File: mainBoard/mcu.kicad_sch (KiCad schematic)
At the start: 36 parts, among them J2 USB_A, SW2 SW_SPDT, SW3 SW_Push, SW4 SW_Push, U19 23LC1024-I/ST, U5 USBLC6-2SC6, U6 STM32F413RHT6, Y1 RH100-48.000-10-F-1015-X-TR-N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

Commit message: add NOR flash for UI
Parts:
- added C55: 100nF, Capacitor_SMD:C_0603_1608Metric_Pad1.08x0.95mm_HandSolder, symbol Device:C
- added U22: W25Q64JVSSIM TR, Package_SO:SOIC-8_5.3x5.3mm_P1.27mm, symbol Memory_Flash:W25Q16JVSS
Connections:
- net +3.3V: now also C55.1, U22.8 (VCC)
- net GND: now also C55.2, U22.4 (GND)
- net QSPI_SCK: now also U22.6 (CLK)
- net QSPI_SIO0: now also U22.5 (DI/IO_{0})
- net QSPI_SIO1: now also U22.2 (DO/IO_{1})
- net QSPI_SIO2: now also U22.3 (~{WP}/IO_{2})
- net QSPI_SIO3: now also U22.7 (~{HOLD}/~{RESET}/IO_{3})
- new net QSPI_ROM_CS: U22.1 (~{CS})
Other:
- note added: "8MB NOR Flash"
- moved on the sheet: C21, C22, C23, C24, C25, C26, C27, C28, C29, C30, C31, R18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

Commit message: change to 16MB ROM
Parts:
- U22: value W25Q64JVSSIM TR -> W25Q128JVSIQ TR
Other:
- note added: "16MB NOR Flash"
- note removed: "8MB NOR Flash"
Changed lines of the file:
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@@
 		)
 	)
-	(text "8MB NOR Flash"
+	(text "16MB NOR Flash"
 		(exclude_from_sim no)
 		(at 85.852 146.812 0)
@@
 			)
 		)
-		(property "Value" "W25Q64JVSSIM TR"
+		(property "Value" "W25Q128JVSIQ TR"
 			(at 71.12 123.1899 0)
 			(show_name no)

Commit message: working on pcb layout, change to soic sram
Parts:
- U19: value 23LC1024-I/ST -> 23LC1024-E/SN; footprint Package_SO:TSSOP-8_4.4x3mm_P0.65mm -> Package_SO:SOIC-8_5.3x5.3mm_P1.27mm
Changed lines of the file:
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@@
 			)
 		)
-		(property "Value" "23LC1024-I/ST"
+		(property "Value" "23LC1024-E/SN"
 			(at 64.135 180.975 0)
 			(show_name no)
@@
 			)
 		)
-		(property "Footprint" "Package_SO:TSSOP-8_4.4x3mm_P0.65mm"
+		(property "Footprint" "Package_SO:SOIC-8_5.3x5.3mm_P1.27mm"
 			(at 55.88 195.58 0)
 			(hide yes)

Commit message: work on layout
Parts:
- removed NT2: NetTie_2, NetTie:NetTie-2_SMD_Pad0.5mm, symbol Device:NetTie_2
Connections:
- net HSE_GND is gone; now on net GND: C22.2, C23.2
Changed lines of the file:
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@@
 	(wire
 		(pts
+			(xy 196.85 179.07) (xy 196.85 185.42)
+		)
+		(stroke
+			(width 0)
+			(type default)
+		)
+	)
+	(wire
+		(pts
 			(xy 157.48 111.76) (xy 153.67 111.76)
 		)
@@
 	(wire
 		(pts
-			(xy 196.85 179.07) (xy 196.85 180.34)
-		)
-		(stroke
-			(width 0)
-			(type default)
-		)
-	)
-	(wire
-		(pts
 			(xy 45.72 237.49) (xy 57.15 237.49)
 		)
@@
 					(unit 1)
 				)
-			)
-		)
-	)
-	(symbol
-		(lib_id "Device:NetTie_2")
-		(at 196.85 182.88 90)
-		(unit 1)
-		(body_style 1)
-		(exclude_from_sim no)
-		(in_bom no)
-		(on_board yes)
-		(in_pos_files yes)
-		(dnp no)
-		(fields_autoplaced yes)
-		(property "Reference" "NT2"
-			(at 191.77 182.88 0)
-			(hide yes)
-			(show_name no)
-			(do_not_autoplace no)
-			(effects
-				(font
-					(size 1.27 1.27)
-				)
-			)
-		)
-		(property "Value" "NetTie_2"
-			(at 194.31 182.88 0)
-			(hide yes)
-			(show_name no)
-			(do_not_autoplace no)
-			(effects
-				(font
-					(size 1.27 1.27)
-				)
-			)
-		)
-		(property "Footprint" "NetTie:NetTie-2_SMD_Pad0.5mm"
-			(at 196.85 182.88 0)
-			(hide yes)
-			(show_name no)
-			(do_not_autoplace no)
-			(effects
-				(font
-					(size 1.27 1.27)
-				)
-			)
-		)
-		(property "Datasheet" ""
-			(at 196.85 182.88 0)
-			(hide yes)
-			(show_name no)
-			(do_not_autoplace no)
-			(effects
-				(font
-					(size 1.27 1.27)
-				)
-			)
-		)
-		(property "Description" "Net tie, 2 pins"
-			(at 196.85 182.88 0)
-			(hide yes)
-			(show_name no)
-			(do_not_autoplace no)
-			(effects
-				(font
-					(size 1.27 1.27)
-				)
-			)
-		)
-		(pin "1"
-		)
-		(pin "2"
-		)
-		(instances
-			(project "mainBoard"
-				(path "/0650c7a8-acba-429c-9f8e-eec0baf0bc1c/fede4c36-00cc-4d3d-b71c-5243ba232202/7d5a1283-086b-46b0-8df7-a9850521fb5e"
-					(reference "NT2")
-					(unit 1)
-				)

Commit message: work on layout
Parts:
- removed NT1: NetTie_2, NetTie:NetTie-2_SMD_Pad0.5mm, symbol Device:NetTie_2
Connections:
- net STM_VREF is gone; now on net +3.3VA: U6.13 (VREF+)
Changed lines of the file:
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@@
 	(wire
 		(pts
-			(xy 140.97 129.54) (xy 142.24 129.54)
+			(xy 140.97 129.54) (xy 266.7 129.54)
 		)
 		(stroke
@@
 	(wire
 		(pts
-			(xy 147.32 129.54) (xy 266.7 129.54)
-		)
-		(stroke
-			(width 0)
-			(type default)
-		)
-	)
-	(wire
-		(pts
 			(xy 250.19 66.04) (xy 250.19 67.31)
 		)
@@
 					(unit 1)
 				)
-			)
-		)
-	)
-	(symbol
-		(lib_id "Device:NetTie_2")
-		(at 144.78 129.54 180)
-		(unit 1)
-		(body_style 1)
-		(exclude_from_sim no)
-		(in_bom no)
-		(on_board yes)
-		(in_pos_files yes)
-		(dnp no)
-		(fields_autoplaced yes)
-		(property "Reference" "NT1"
-			(at 144.78 134.62 0)
-			(hide yes)
-			(show_name no)
-			(do_not_autoplace no)
-			(effects
-				(font
-					(size 1.27 1.27)
-				)
-			)
-		)
-		(property "Value" "NetTie_2"
-			(at 144.78 132.08 0)
-			(hide yes)
-			(show_name no)
-			(do_not_autoplace no)
-			(effects
-				(font
-					(size 1.27 1.27)
-				)
-			)
-		)
-		(property "Footprint" "NetTie:NetTie-2_SMD_Pad0.5mm"
-			(at 144.78 129.54 0)
-			(hide yes)
-			(show_name no)
-			(do_not_autoplace no)
-			(effects
-				(font
-					(size 1.27 1.27)
-				)
-			)
-		)
-		(property "Datasheet" ""
-			(at 144.78 129.54 0)
-			(hide yes)
-			(show_name no)
-			(do_not_autoplace no)
-			(effects
-				(font
-					(size 1.27 1.27)
-				)
-			)
-		)
-		(property "Description" "Net tie, 2 pins"
-			(at 144.78 129.54 0)
-			(hide yes)
-			(show_name no)
-			(do_not_autoplace no)
-			(effects
-				(font
-					(size 1.27 1.27)
-				)
-			)
-		)
-		(pin "1"
-		)
-		(pin "2"
-		)
-		(instances
-			(project "mainBoard"
-				(path "/0650c7a8-acba-429c-9f8e-eec0baf0bc1c/fede4c36-00cc-4d3d-b71c-5243ba232202/7d5a1283-086b-46b0-8df7-a9850521fb5e"
-					(reference "NT1")
-					(unit 1)
-				)

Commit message: work on board layout
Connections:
- net TC3_ADC: now also U6.24 (PC4); no longer U6.26 (PB0)
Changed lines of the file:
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@@
 	(global_label "TC3_ADC"
 		(shape input)
-		(at 302.26 162.56 0)
+		(at 266.7 157.48 180)
 		(fields_autoplaced yes)
 		(effects
@@
 				(size 1.27 1.27)
 			)
-			(justify left)
+			(justify right)
 		)
 		(property "Intersheetrefs" "${INTERSHEET_REFS}"
-			(at 311.8581 162.56 0)
+			(at 255.6715 157.48 0)
 			(hide yes)
 			(show_name no)
@@
 					(size 1.27 1.27)
 				)
-				(justify left)
+				(justify right)
 			)
 		)

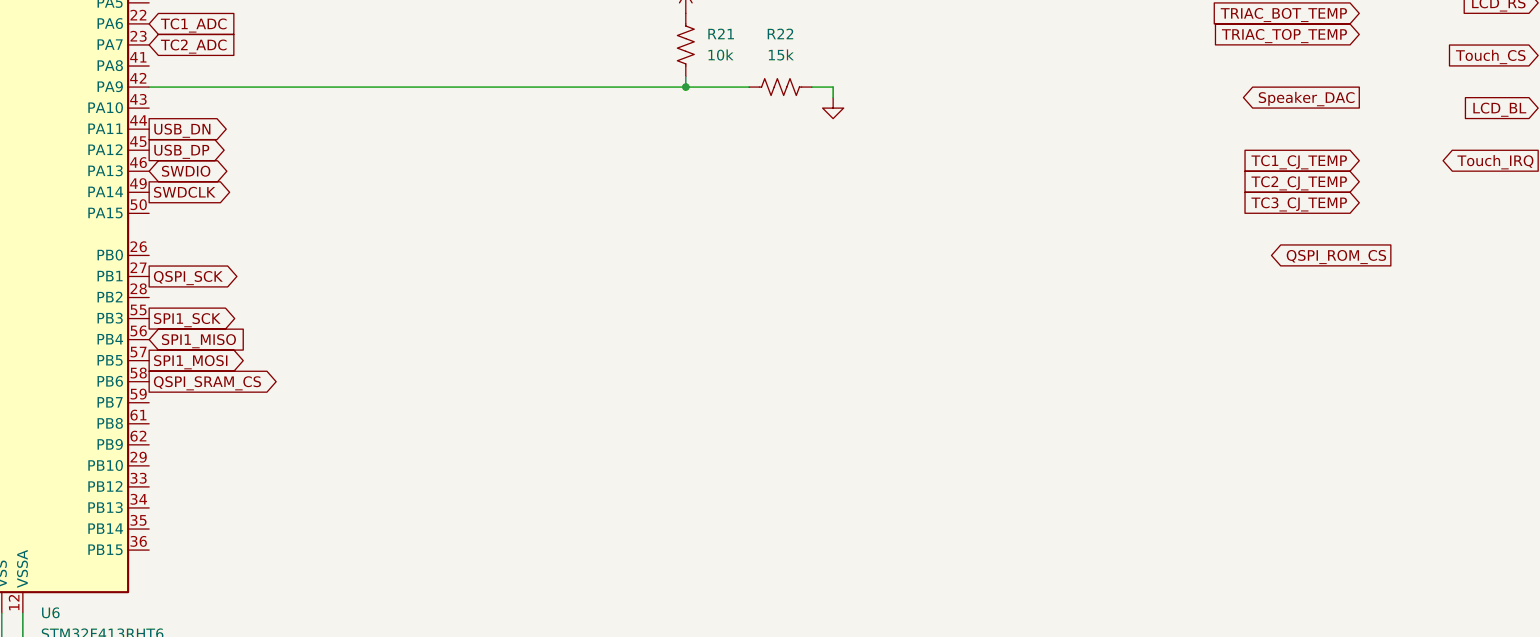
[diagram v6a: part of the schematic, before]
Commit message: layout ADC inputs and DS18B20s
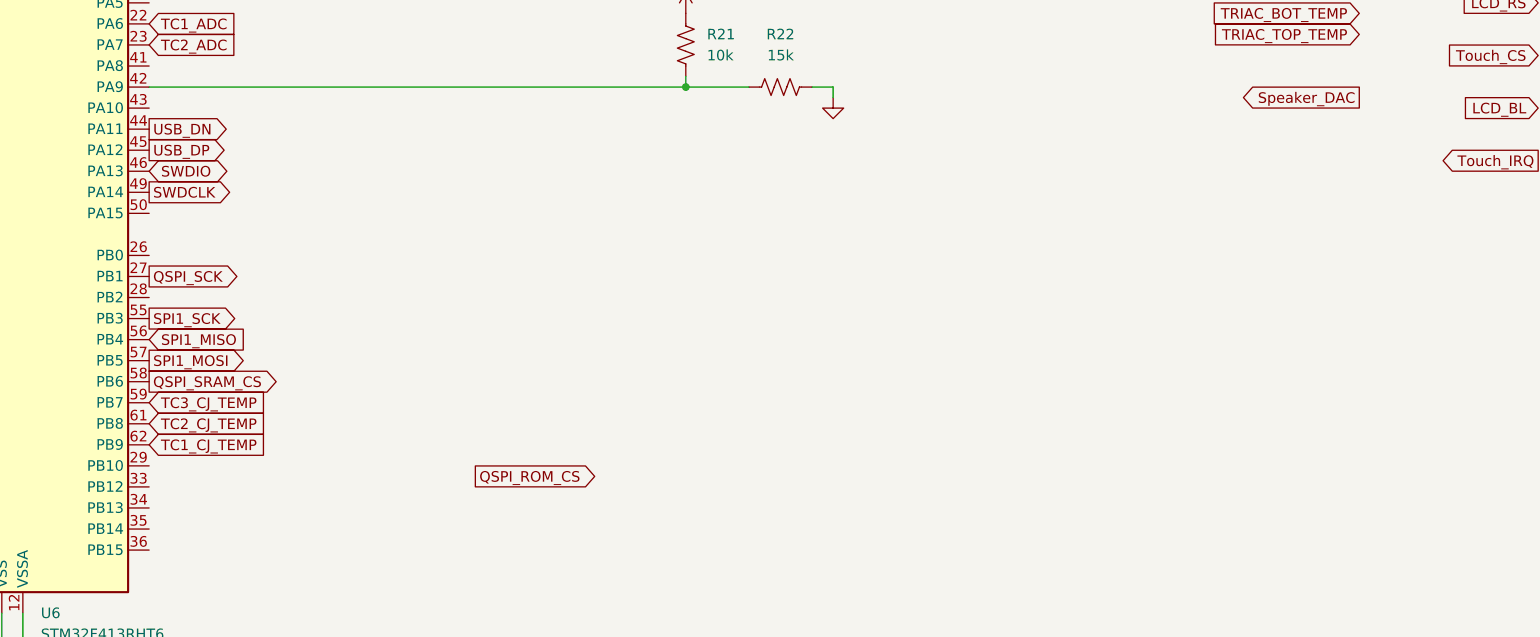
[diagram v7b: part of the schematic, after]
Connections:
- net TC1_CJ_TEMP: now also U6.62 (PB9)
- net TC2_CJ_TEMP: now also U6.61 (PB8)
- net TC3_CJ_TEMP: now also U6.59 (PB7)
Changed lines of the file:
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@@
 	(global_label "TC2_CJ_TEMP"
 		(shape input)
-		(at 448.31 153.67 180)
-		(fields_autoplaced yes)
-		(effects
-			(font
-				(size 1.27 1.27)
-			)
-			(justify right)
-		)
-		(property "Intersheetrefs" "${INTERSHEET_REFS}"
-			(at 434.806 153.67 0)
-			(hide yes)
-			(show_name no)
-			(do_not_autoplace no)
-			(effects
-				(font
-					(size 1.27 1.27)
-				)
-				(justify right)
+		(at 302.26 182.88 0)
+		(fields_autoplaced yes)
+		(effects
+			(font
+				(size 1.27 1.27)
+			)
+			(justify left)
+		)
+		(property "Intersheetrefs" "${INTERSHEET_REFS}"
+			(at 317.7031 182.88 0)
+			(hide yes)
+			(show_name no)
+			(do_not_autoplace no)
+			(effects
+				(font
+					(size 1.27 1.27)
+				)
+				(justify left)
 			)
 		)
@@
 	(global_label "TC1_CJ_TEMP"
 		(shape input)
-		(at 448.31 151.13 180)
-		(fields_autoplaced yes)
-		(effects
-			(font
-				(size 1.27 1.27)
-			)
-			(justify right)
-		)
-		(property "Intersheetrefs" "${INTERSHEET_REFS}"
-			(at 432.8669 151.13 0)
-			(hide yes)
-			(show_name no)
-			(do_not_autoplace no)
-			(effects
-				(font
-					(size 1.27 1.27)
-				)
-				(justify right)
+		(at 302.26 185.42 0)
+		(fields_autoplaced yes)
+		(effects
+			(font
+				(size 1.27 1.27)
+			)
+			(justify left)
+		)
+		(property "Intersheetrefs" "${INTERSHEET_REFS}"
+			(at 317.7031 185.42 0)
+			(hide yes)
+			(show_name no)
+			(do_not_autoplace no)
+			(effects
+				(font
+					(size 1.27 1.27)
+				)
+				(justify left)
 			)
 		)
@@
 	(global_label "QSPI_ROM_CS"
 		(shape output)
-		(at 452.12 162.56 180)
-		(fields_autoplaced yes)
-		(effects
-			(font
-				(size 1.27 1.27)
-			)
-			(justify right)
-		)
-		(property "Intersheetrefs" "${INTERSHEET_REFS}"
-			(at 436.2534 162.56 0)
-			(hide yes)
-			(show_name no)
-			(do_not_autoplace no)
-			(effects
-				(font
-					(size 1.27 1.27)
-				)
-				(justify right)
+		(at 341.63 189.23 0)
+		(fields_autoplaced yes)
+		(effects
+			(font
+				(size 1.27 1.27)
+			)
+			(justify left)
+		)
+		(property "Intersheetrefs" "${INTERSHEET_REFS}"
+			(at 357.4966 189.23 0)
+			(hide yes)
+			(show_name no)
+			(do_not_autoplace no)
+			(effects
+				(font
+					(size 1.27 1.27)
+				)
+				(justify left)
 			)
 		)
@@
 	(global_label "TC3_CJ_TEMP"
 		(shape input)
-		(at 448.31 156.21 180)
-		(fields_autoplaced yes)
-		(effects
-			(font
-				(size 1.27 1.27)
-			)
-			(justify right)
-		)
-		(property "Intersheetrefs" "${INTERSHEET_REFS}"
-			(at 434.806 156.21 0)
-			(hide yes)
-			(show_name no)
-			(do_not_autoplace no)
-			(effects
-				(font
-					(size 1.27 1.27)
-				)
-				(justify right)
-			)
-		)
+		(at 302.26 180.34 0)
+		(fields_autoplaced yes)
+		(effects
+			(font
+				(size 1.27 1.27)
+			)
+			(justify left)
+		)
+		(property "Intersheetrefs" "${INTERSHEET_REFS}"
+			(at 317.7031 180.34 0)
+			(hide yes)
+			(show_name no)
+			(do_not_autoplace no)
+			(effects
+				(font
+					(size 1.27 1.27)
+				)
+				(justify left)
+			)
+		)
